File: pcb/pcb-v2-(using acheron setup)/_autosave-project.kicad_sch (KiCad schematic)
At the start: 174 parts, among them J1 Conn_01x22_Female, J2 Conn_01x22_Male, J3 Conn_01x03_Male, J4 helios, SW1 CherryMX, SW10 CherryMX, SW11 CherryMX, SW12 CherryMX, SW13 CherryMX, SW14 CherryMX, SW15 CherryMX, SW16 CherryMX, SW17 CherryMX, SW18 CherryMX, SW19 CherryMX, SW2 CherryMX, SW20 CherryMX, SW21 CherryMX, SW22 CherryMX, SW23 CherryMX, SW24 CherryMX, SW25 CherryMX, SW26 CherryMX, SW27 CherryMX, SW28 CherryMX, SW29 CherryMX, SW3 CherryMX, SW30 CherryMX, SW31 CherryMX, SW32 CherryMX, SW33 CherryMX, SW34 CherryMX, SW35 CherryMX, SW36 CherryMX, SW37 CherryMX, SW38 CherryMX, SW39 CherryMX, SW4 CherryMX, SW40 CherryMX, SW41 CherryMX, SW42 CherryMX, SW43 CherryMX, SW44 CherryMX, SW45 CherryMX, SW46 CherryMX, SW47 CherryMX, SW48 CherryMX, SW49 CherryMX, SW5 CherryMX, SW50 CherryMX, SW51 CherryMX, SW52 CherryMX, SW53 CherryMX, SW54 CherryMX, SW55 CherryMX, SW56 CherryMX, SW57 CherryMX, SW58 CherryMX, SW59 CherryMX, SW6 CherryMX, SW60 CherryMX, SW61 CherryMX, SW62 CherryMX, SW63 CherryMX, SW64 CherryMX, SW65 CherryMX, SW66 CherryMX, SW67 CherryMX, SW68 CherryMX, SW69 CherryMX, SW7 CherryMX, SW70 CherryMX, SW71 CherryMX, SW72 CherryMX, SW73 CherryMX, SW74 CherryMX, SW75 CherryMX, SW76 CherryMX, SW77 CherryMX, SW78 CherryMX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

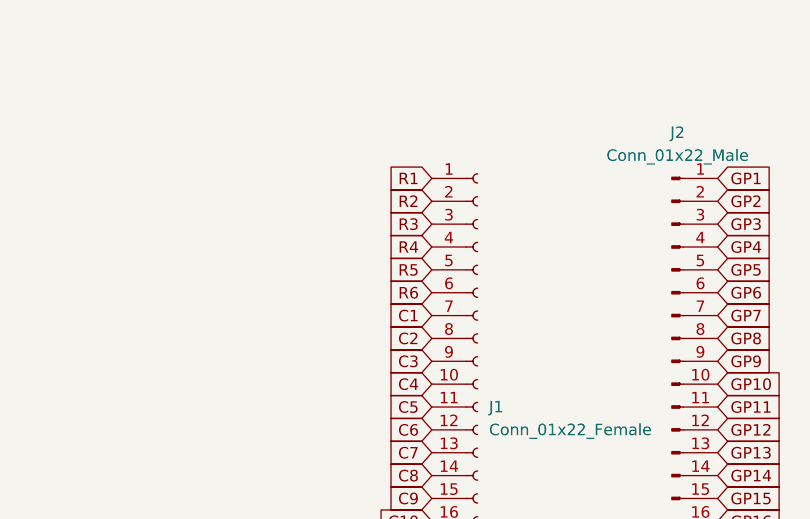
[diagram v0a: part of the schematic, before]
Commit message: routing v1 done and space bar stab added
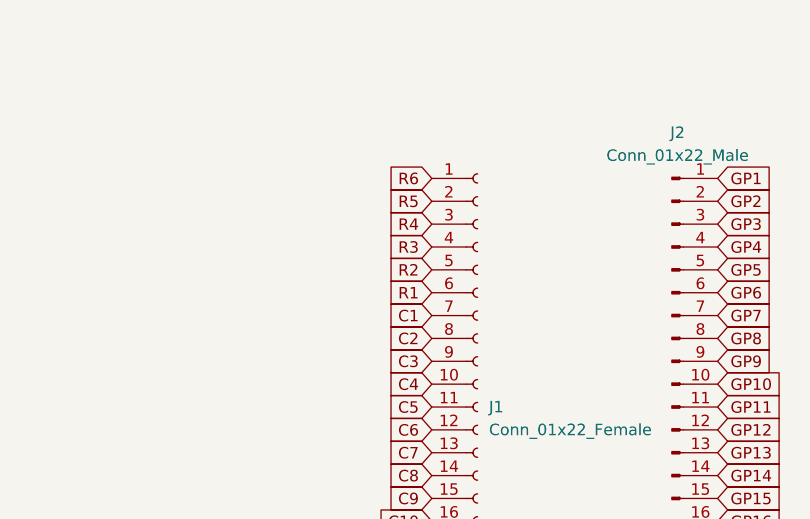
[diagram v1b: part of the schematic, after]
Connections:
- net R1: now also J1.6 (Pin_6); no longer J1.1 (Pin_1)
- net R2: now also J1.5 (Pin_5); no longer J1.2 (Pin_2)
- net R3: now also J1.4 (Pin_4); no longer J1.3 (Pin_3)
- net R4: now also J1.3 (Pin_3); no longer J1.4 (Pin_4)
- net R5: now also J1.2 (Pin_2); no longer J1.5 (Pin_5)
- net R6: now also J1.1 (Pin_1); no longer J1.6 (Pin_6)
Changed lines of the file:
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@@
     )
   )
-  (global_label "R5" (shape input) (at 295.91 69.85 180) (fields_autoplaced)
-    (effects (font (size 1.27 1.27)) (justify right))
-    (property "Intersheet References" "${INTERSHEET_REFS}" (id 0) (at 291.0174 69.7706 0)
+  (global_label "R5" (shape input) (at 295.91 62.23 180) (fields_autoplaced)
+    (effects (font (size 1.27 1.27)) (justify right))
+    (property "Intersheet References" "${INTERSHEET_REFS}" (id 0) (at 291.0174 62.3094 0)
       (effects (font (size 1.27 1.27)) (justify right) hide)
     )
@@
     )
   )
-  (global_label "R2" (shape input) (at 295.91 62.23 180) (fields_autoplaced)
-    (effects (font (size 1.27 1.27)) (justify right))
-    (property "Intersheet References" "${INTERSHEET_REFS}" (id 0) (at 291.0174 62.1506 0)
+  (global_label "R2" (shape input) (at 295.91 69.85 180) (fields_autoplaced)
+    (effects (font (size 1.27 1.27)) (justify right))
+    (property "Intersheet References" "${INTERSHEET_REFS}" (id 0) (at 291.0174 69.9294 0)
       (effects (font (size 1.27 1.27)) (justify right) hide)
     )
@@
     )
   )
-  (global_label "R1" (shape input) (at 295.91 59.69 180) (fields_autoplaced)
-    (effects (font (size 1.27 1.27)) (justify right))
-    (property "Intersheet References" "${INTERSHEET_REFS}" (id 0) (at 291.0174 59.6106 0)
+  (global_label "R1" (shape input) (at 295.91 72.39 180) (fields_autoplaced)
+    (effects (font (size 1.27 1.27)) (justify right))
+    (property "Intersheet References" "${INTERSHEET_REFS}" (id 0) (at 291.0174 72.4694 0)
       (effects (font (size 1.27 1.27)) (justify right) hide)
     )
@@
     )
   )
-  (global_label "R3" (shape input) (at 295.91 64.77 180) (fields_autoplaced)
-    (effects (font (size 1.27 1.27)) (justify right))
-    (property "Intersheet References" "${INTERSHEET_REFS}" (id 0) (at 291.0174 64.6906 0)
+  (global_label "R3" (shape input) (at 295.91 67.31 180) (fields_autoplaced)
+    (effects (font (size 1.27 1.27)) (justify right))
+    (property "Intersheet References" "${INTERSHEET_REFS}" (id 0) (at 291.0174 67.3894 0)
       (effects (font (size 1.27 1.27)) (justify right) hide)
     )
@@
     )
   )
-  (global_label "R6" (shape input) (at 295.91 72.39 180) (fields_autoplaced)
-    (effects (font (size 1.27 1.27)) (justify right))
-    (property "Intersheet References" "${INTERSHEET_REFS}" (id 0) (at 291.0174 72.3106 0)
+  (global_label "R6" (shape input) (at 295.91 59.69 180) (fields_autoplaced)
+    (effects (font (size 1.27 1.27)) (justify right))
+    (property "Intersheet References" "${INTERSHEET_REFS}" (id 0) (at 291.0174 59.7694 0)
       (effects (font (size 1.27 1.27)) (justify right) hide)
     )
@@
     )
   )
-  (global_label "R4" (shape input) (at 295.91 67.31 180) (fields_autoplaced)
-    (effects (font (size 1.27 1.27)) (justify right))
-    (property "Intersheet References" "${INTERSHEET_REFS}" (id 0) (at 291.0174 67.2306 0)
-      (effects (font (size 1.27 1.27)) (justify right) hide)
-    )
+  (global_label "R4" (shape input) (at 295.91 64.77 180) (fields_autoplaced)
+    (effects (font (size 1.27 1.27)) (justify right))
+    (property "Intersheet References" "${INTERSHEET_REFS}" (id 0) (at 291.0174 64.8494 0)
+      (effects (font (size 1.27 1.27)) (justify right) hide)
+    )
